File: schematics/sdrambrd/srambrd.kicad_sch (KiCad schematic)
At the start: 13 parts, among them J1 LEFT, J2 Micro_SD_Card, U1 IS61LV25616AL

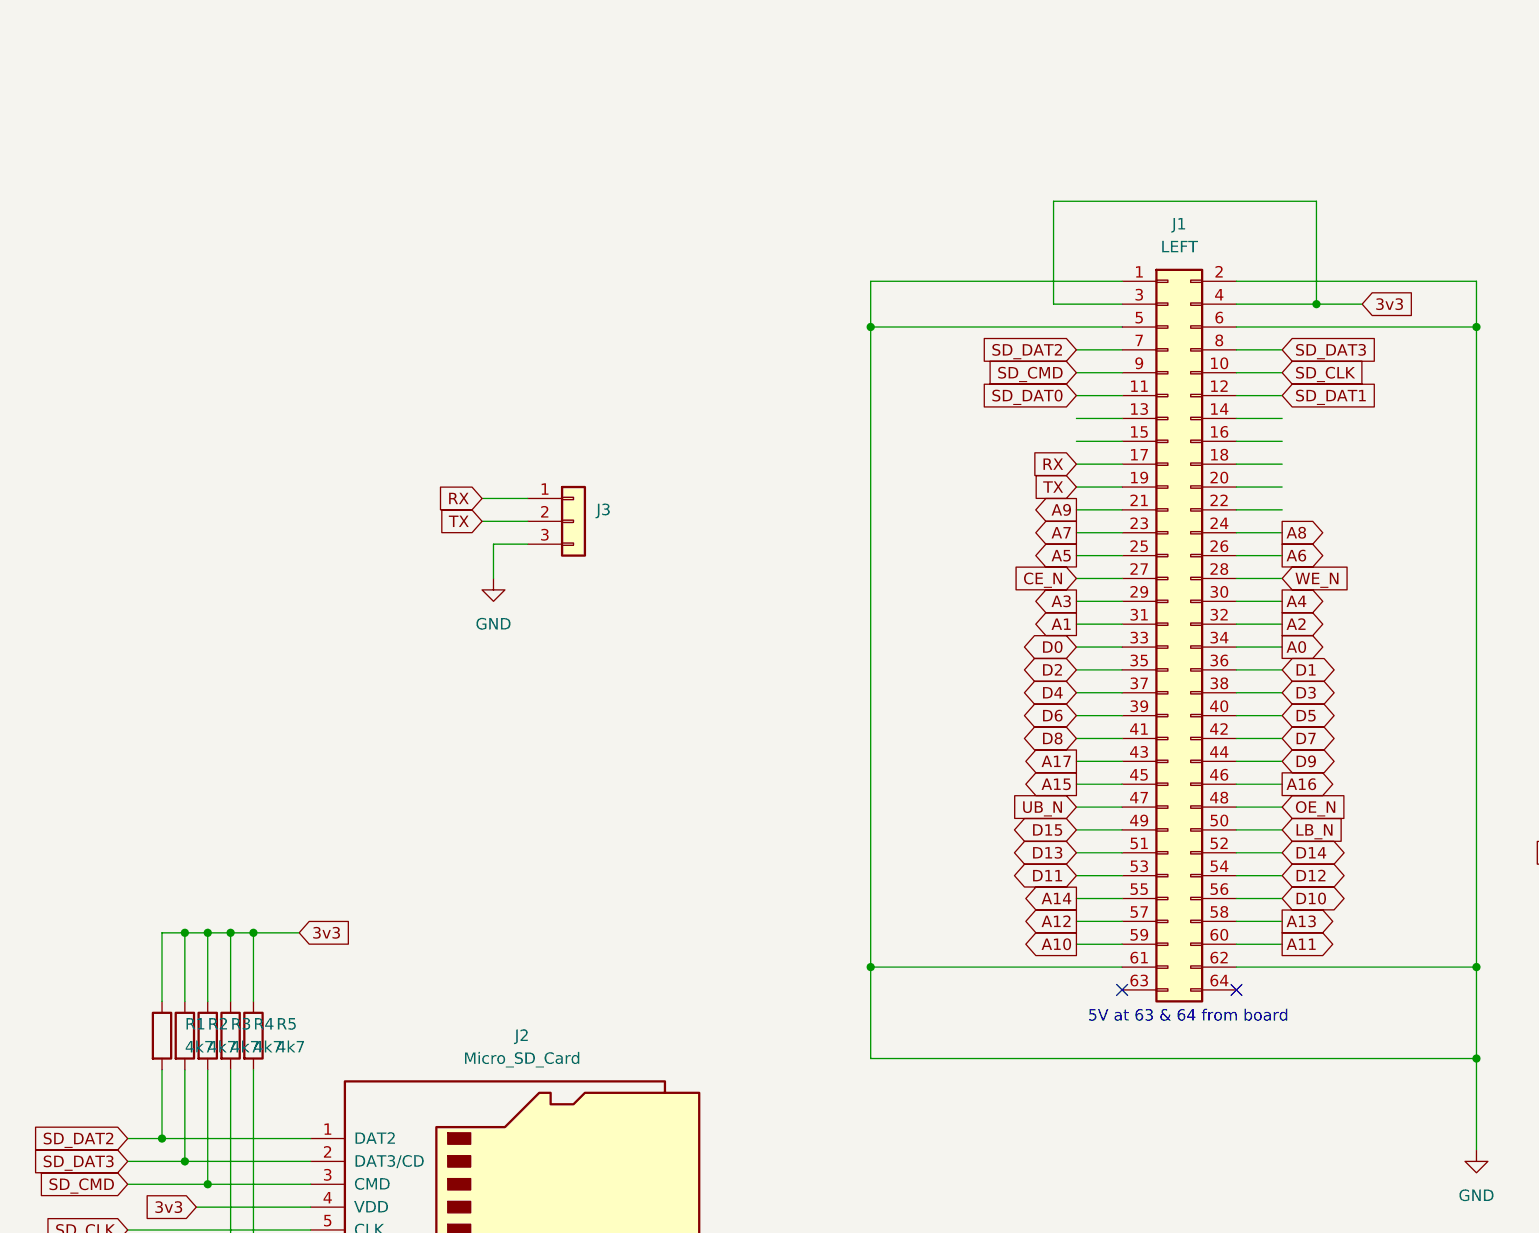
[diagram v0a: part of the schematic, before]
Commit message: Rv32: Updated SRAM brd schematic. Also updated legend in lcdbrd.
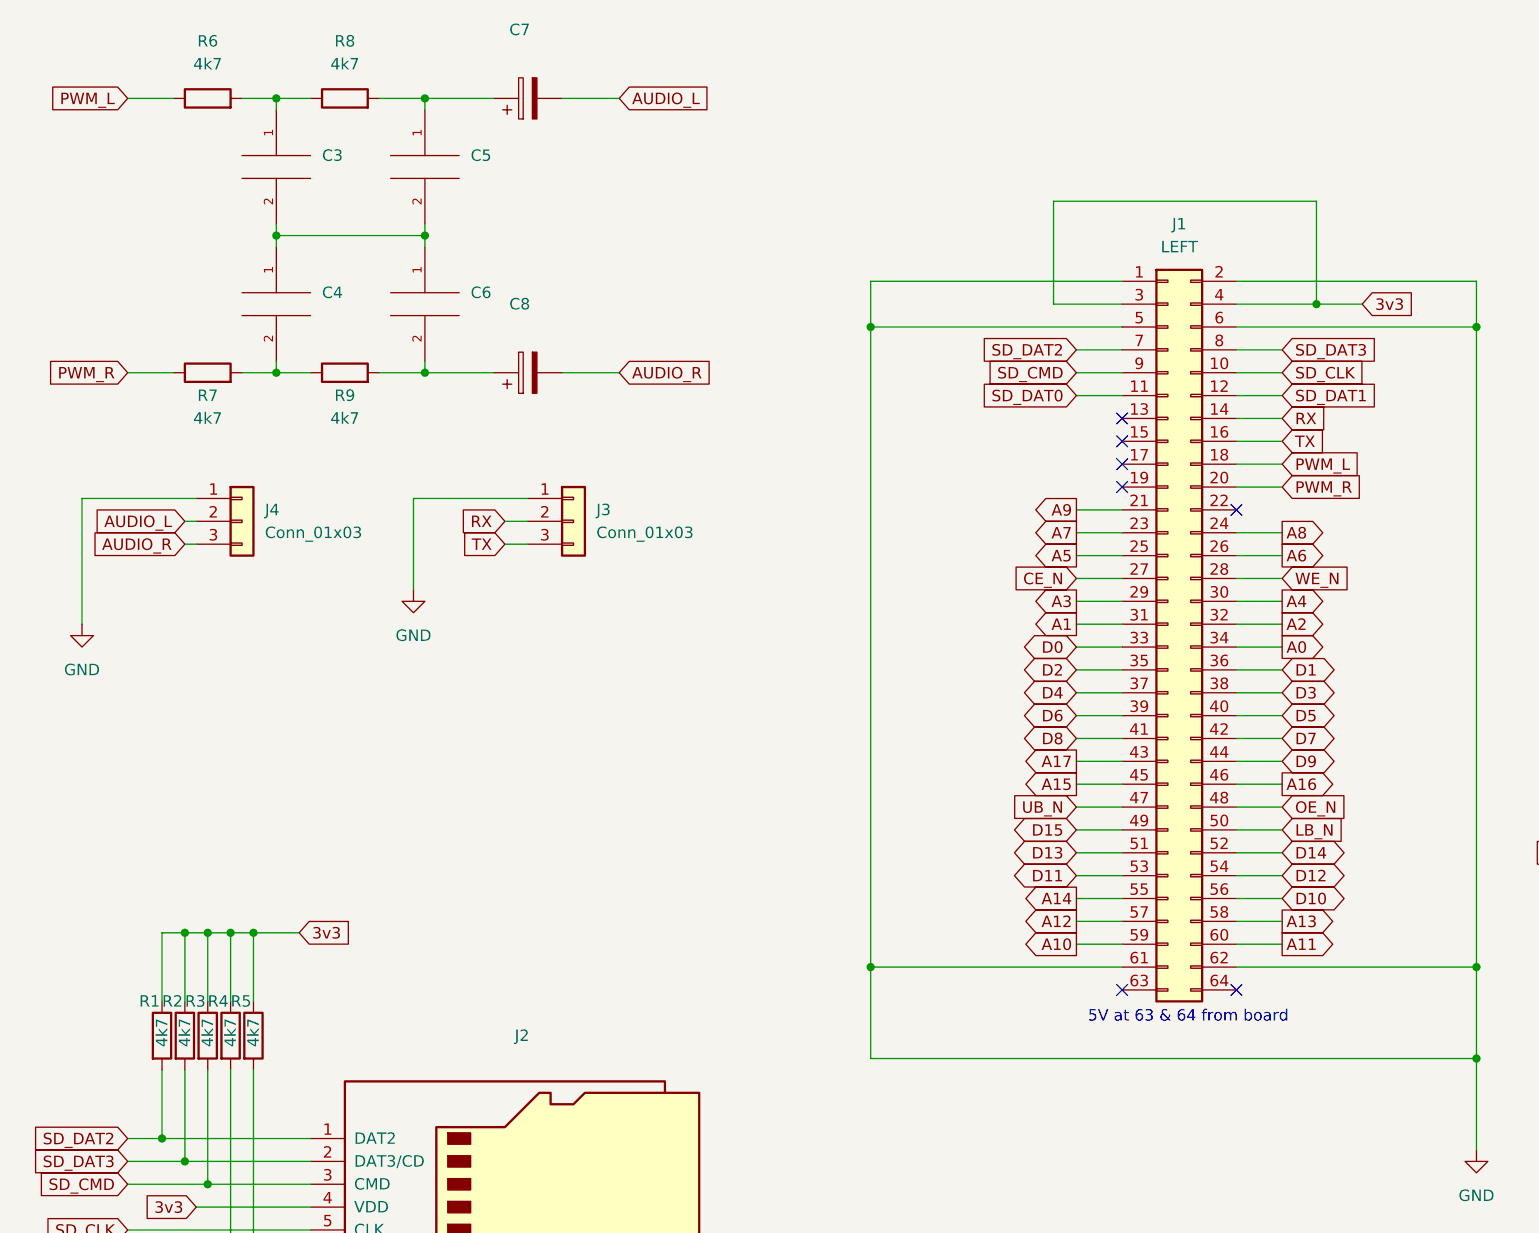
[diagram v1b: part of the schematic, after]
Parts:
- added C3, C4, C5, C6: (no value), Capacitor_SMD:C_0805_2012Metric_Pad1.18x1.45mm_HandSolder, symbol pspice:C
- added C7, C8: (no value), symbol Device:C_Polarized
- added J4: Conn_01x03, Connector_PinHeader_2.54mm:PinHeader_1x03_P2.54mm_Vertical, symbol Connector_Generic:Conn_01x03
- added R6, R7, R8, R9: 4k7, Resistor_SMD:R_0805_2012Metric_Pad1.20x1.40mm_HandSolder, symbol Device:R
- J2: value Micro_SD_Card -> (none); footprint Connector_Card:microSD_HC_Hirose_DM3BT-DSF-PEJS -> (none)
- J3: value (none) -> Conn_01x03; footprint (none) -> Connector_PinHeader_2.54mm:PinHeader_1x03_P2.54mm_Vertical
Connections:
- net GND: now also J3.1 (Pin_1), J4.1 (Pin_1); no longer J3.3 (Pin_3)
- net RX: now also J1.14 (Pin_14), J3.2 (Pin_2); no longer J1.17 (Pin_17), J3.1 (Pin_1)
- net TX: now also J1.16 (Pin_16), J3.3 (Pin_3); no longer J1.19 (Pin_19), J3.2 (Pin_2)
- net PWM_L: now reaches J1.18 (Pin_18)
- net PWM_L: now also R6.1
- net PWM_R: now reaches J1.20 (Pin_20)
- net PWM_R: now also R7.1
- new net: C3.1, R6.2, R8.1
- new net: C3.2, C4.1, C5.2, C6.1
- new net: C4.2, R7.2, R9.1
- new net: C6.2, C8.1, R9.2
- new net: C5.1, C7.1, R8.2
- new net AUDIO_L: C7.2, J4.2 (Pin_2)
- new net AUDIO_R: C8.2, J4.3 (Pin_3)
- no-connect marks 2 -> 7

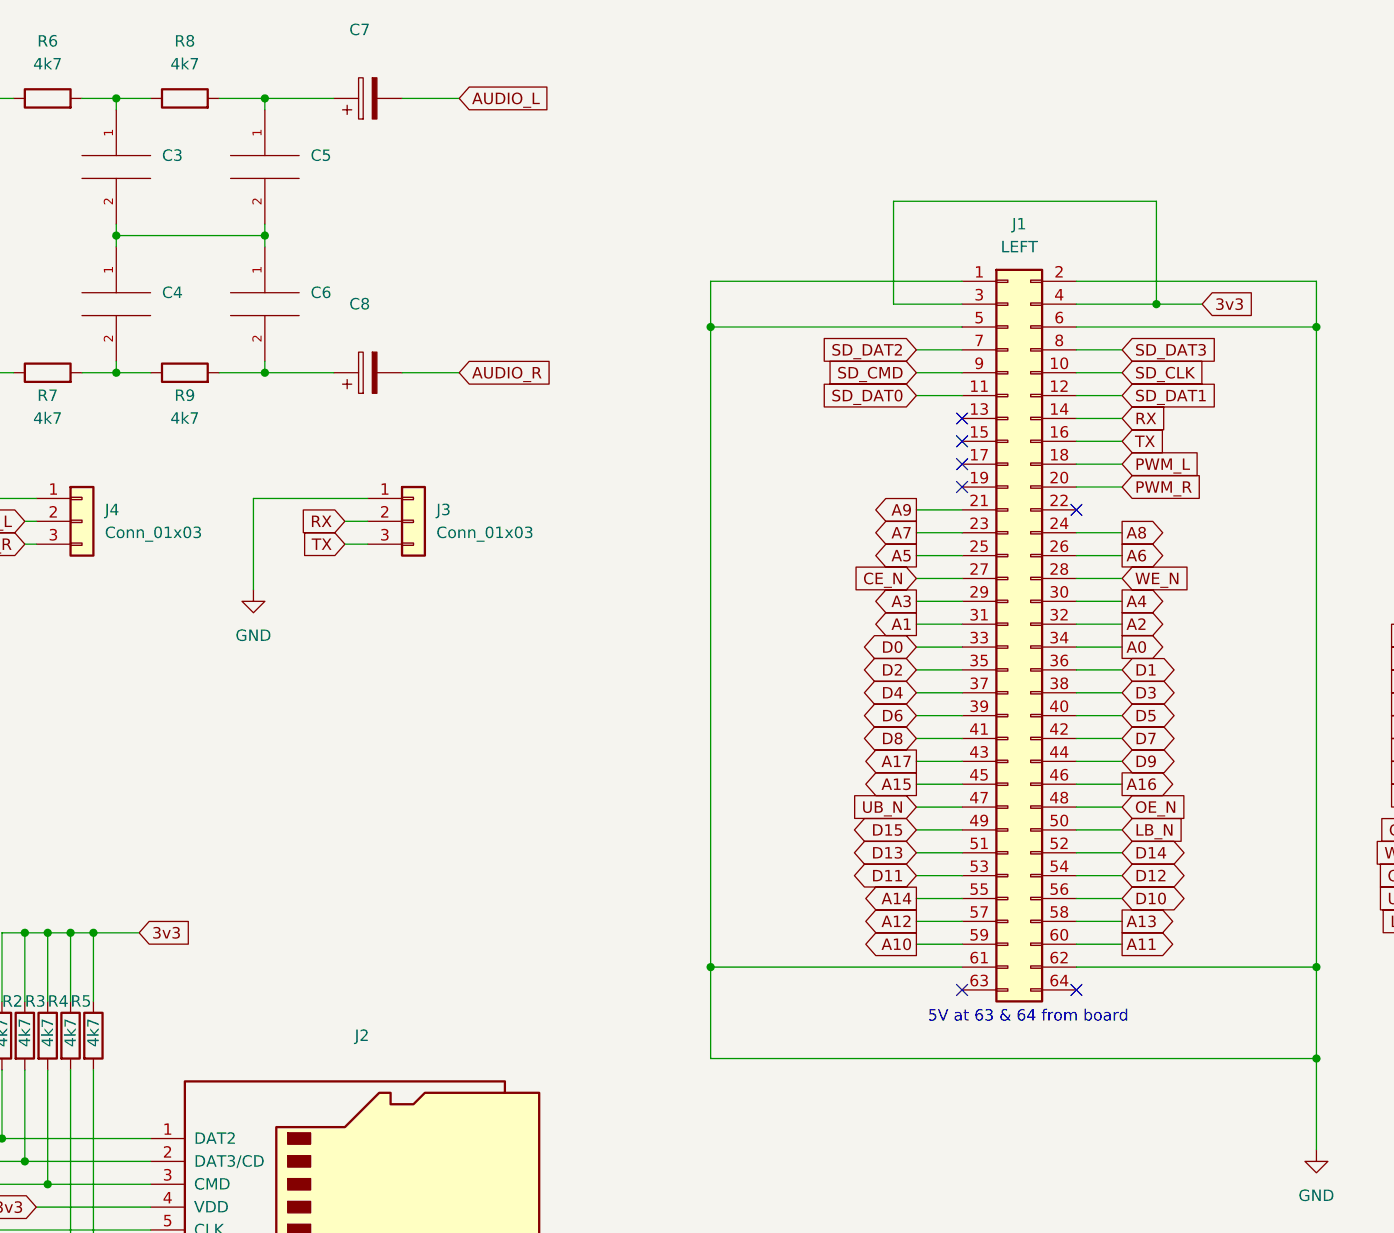
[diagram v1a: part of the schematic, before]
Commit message: Rv32: SRAM Aux board schematics updated. JLCPCB v1
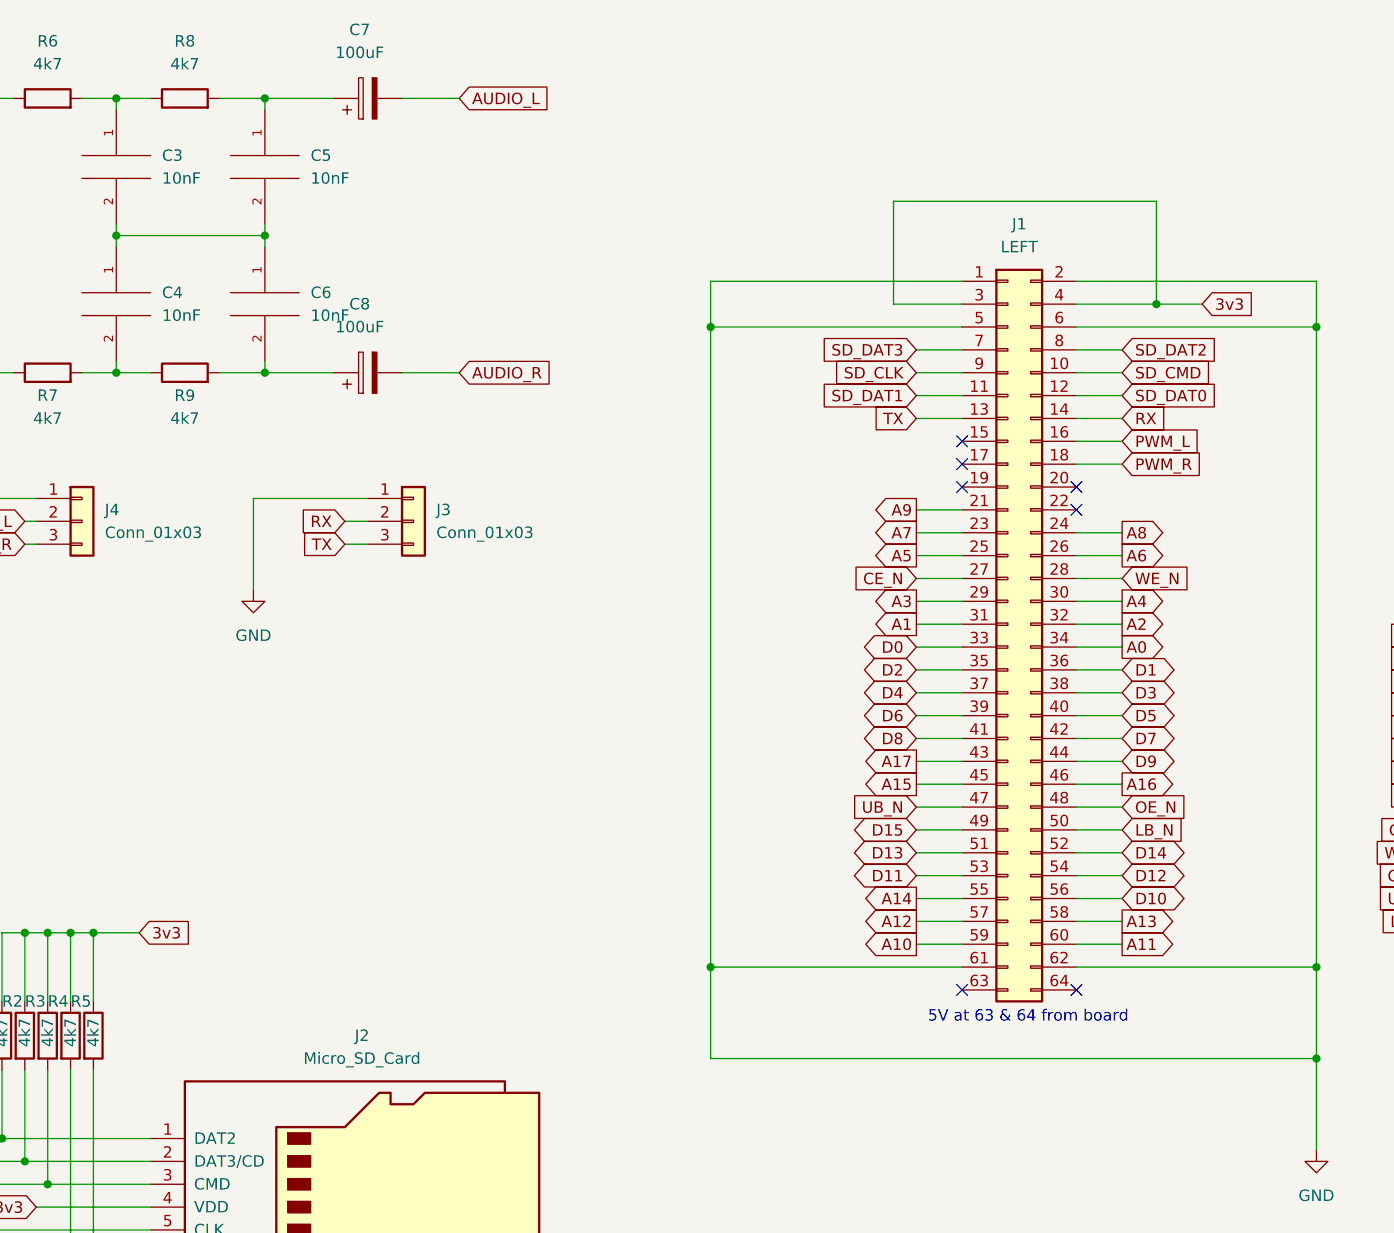
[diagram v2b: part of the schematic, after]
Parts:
- C3, C4, C5, C6: value (none) -> 10nF
- C7, C8: value (none) -> 100uF; footprint (none) -> Capacitor_SMD:CP_Elec_5x5.3
- J2: value (none) -> Micro_SD_Card; footprint (none) -> Connector_Card:microSD_HC_Hirose_DM3D-SF
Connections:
- net PWM_L: now also J1.16 (Pin_16); no longer J1.18 (Pin_18)
- net PWM_R: now also J1.18 (Pin_18); no longer J1.20 (Pin_20)
- net SD_CLK: now also J1.9 (Pin_9); no longer J1.10 (Pin_10)
- net SD_CMD: now also J1.10 (Pin_10); no longer J1.9 (Pin_9)
- net SD_DAT0: now also J1.12 (Pin_12); no longer J1.11 (Pin_11)
- net SD_DAT1: now also J1.11 (Pin_11); no longer J1.12 (Pin_12)
- net SD_DAT2: now also J1.8 (Pin_8); no longer J1.7 (Pin_7)
- net SD_DAT3: now also J1.7 (Pin_7); no longer J1.8 (Pin_8)
- net TX: now also J1.13 (Pin_13); no longer J1.16 (Pin_16)

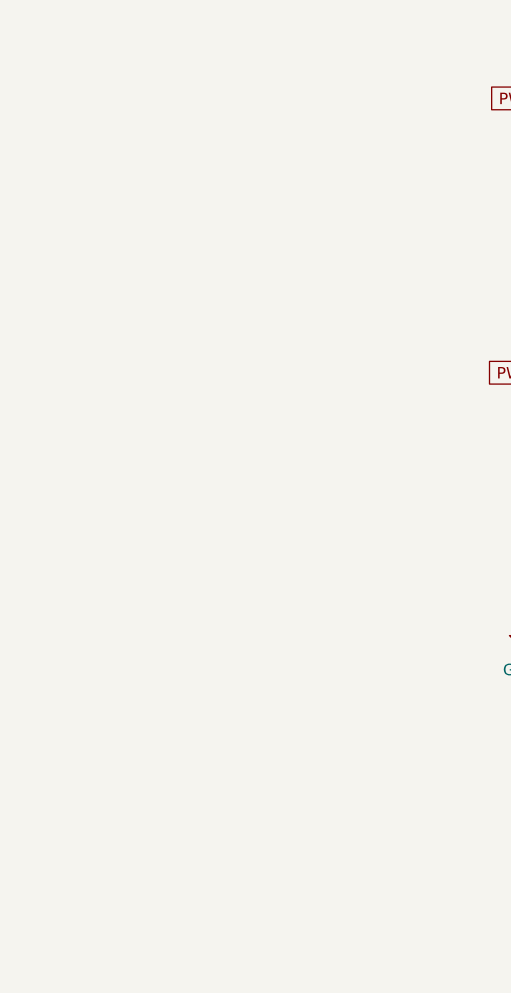
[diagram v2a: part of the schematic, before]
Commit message: Rv32: Added some legend to SRAM board schematics.
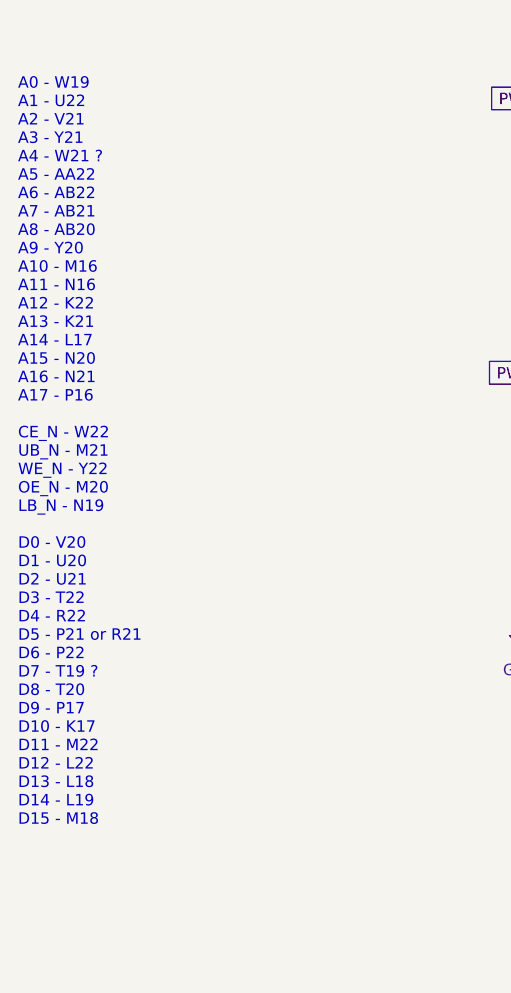
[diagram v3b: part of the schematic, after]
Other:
- note added: "A0 - W19 A1 - U22 A2 - V21 A3 - Y21 A4 - W21 ? A5 - AA22 A6 - AB22 A7 - AB21 A8 - AB20 A9 - Y20 A10 - M16 A11 - N16 A12 - K22 A13 - K21 A14 - L17 A15 - N20 A16 - N21 A17 - P16 CE_N - W22 UB_N - M21 WE_N - Y22 OE_N - M20 LB_N - N19 D0 - V20 D1 - U20 D2 - U21 D3 - T22 D4 - R22 D5 - P21 or R21 D6 - P22 D7 - T19 ? D8 - T20 D9 - P17 D10 - K17 D11 - M22 D12 - L22 D13 - L18 D14 - L19 D15 - M18"
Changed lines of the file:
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@@
+    (effects (font (size 1.27 1.27)) (justify left bottom))
+  )
+  (text "A0 - W19\nA1 - U22\nA2 - V21\nA3 - Y21\nA4 - W21 ?\nA5 - AA22\nA6 - AB22\nA7 - AB21\nA8 - AB20\nA9 - Y20\nA10 - M16\nA11 - N16\nA12 - K22\nA13 - K21\nA14 - L17\nA15 - N20\nA16 - N21\nA17 - P16\n\nCE_N - W22\nUB_N - M21\nWE_N - Y22\nOE_N - M20\nLB_N - N19\n\nD0 - V20\nD1 - U20\nD2 - U21\nD3 - T22\nD4 - R22\nD5 - P21 or R21\nD6 - P22\nD7 - T19 ?\nD8 - T20\nD9 - P17\nD10 - K17\nD11 - M22\nD12 - L22\nD13 - L18\nD14 - L19\nD15 - M18\n\n\n"
+    (at -30.48 110.49 0)
     (effects (font (size 1.27 1.27)) (justify left bottom))
   )
